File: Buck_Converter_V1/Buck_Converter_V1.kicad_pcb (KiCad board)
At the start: 2 copper layers, 75 x 40 mm, 28 parts, among them J1 Conn_01x01_Male, J2 Conn_01x01_Male, J3 Conn_01x01_Male, J4 Conn_01x01_Male, Q1 SI2319CDS-T1-GE3, U1 TL5001CDR

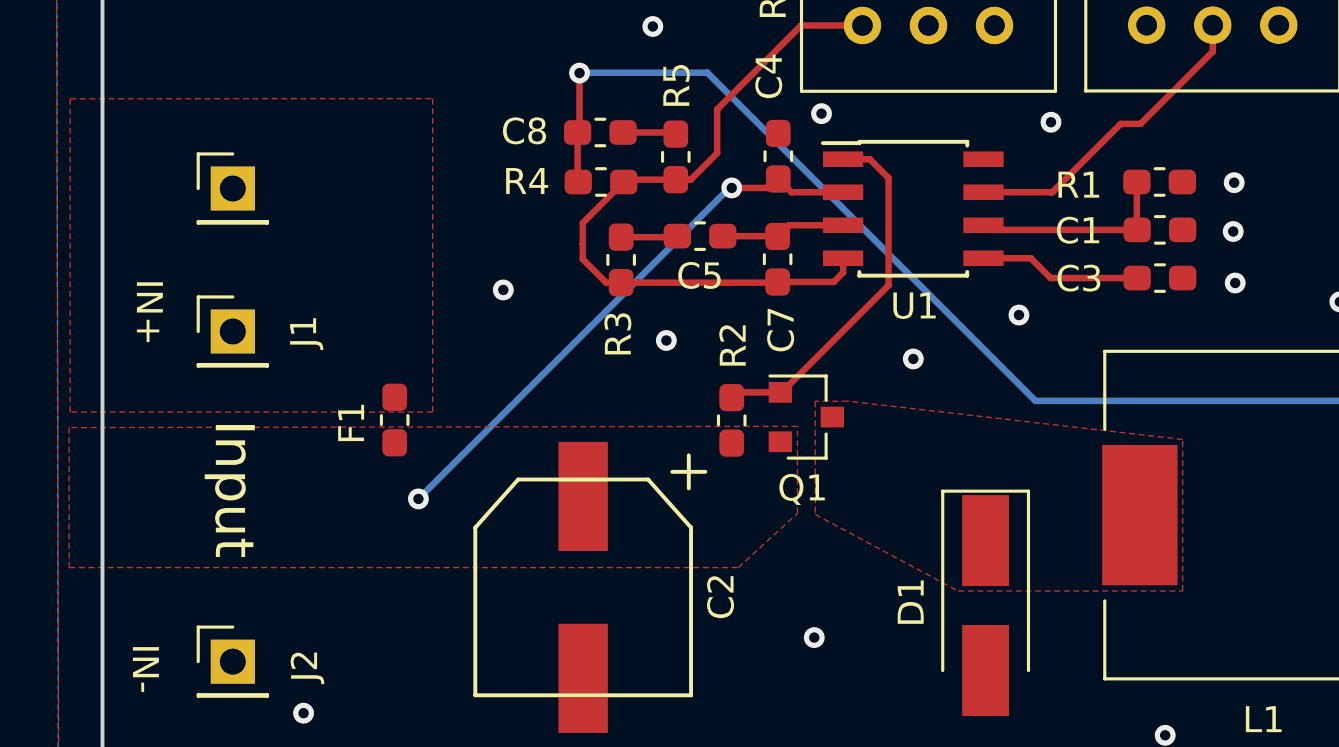
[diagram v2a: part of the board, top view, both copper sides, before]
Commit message: Changed footprint for PMOS switch. Generated gerber files.
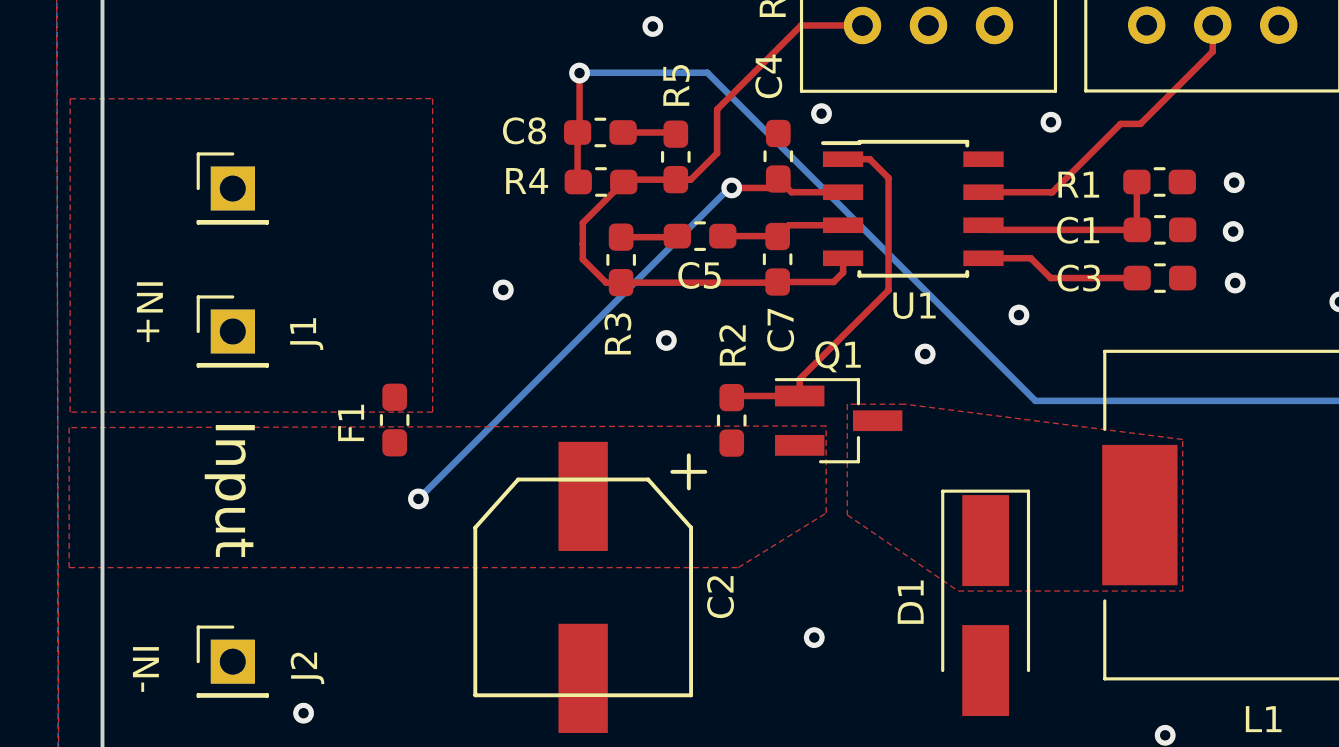
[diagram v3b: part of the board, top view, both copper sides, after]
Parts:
- Q1: footprint Package_TO_SOT_SMD:SOT-23 -> Package_TO_SOT_SMD:SOT-23_Handsoldering
- moved Q1 1.25 mm to (137.1, 89.2)
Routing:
- net P_DRIVE: track 14.0 -> 14.8 mm
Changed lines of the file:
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@@
     (thickness 1.6)
     (drawings 10)
-    (tracks 85)
+    (tracks 87)
     (zones 0)
     (modules 28)
@@
     (34 B.Paste user)
     (35 F.Paste user)
-    (36 B.SilkS user hide)
+    (36 B.SilkS user)
     (37 F.SilkS user)
     (38 B.Mask user)
@@
     (visible_elements FFFFFF7F)
     (pcbplotparams
-      (layerselection 0x010fc_ffffffff)
+      (layerselection 0x010f0_ffffffff)
       (usegerberextensions false)
       (usegerberattributes false)
@@
       (psa4output false)
       (plotreference true)
-      (plotvalue true)
+      (plotvalue false)
       (plotinvisibletext false)
       (padsonsilk false)
@@
       (outputformat 1)
       (mirror false)
-      (drillshape 1)
+      (drillshape 0)
       (scaleselection 1)
-      (outputdirectory ""))
+      (outputdirectory "Gerber/"))
   )
   (net 0 "")
@@
     )
   )
-  (module Package_TO_SOT_SMD:SOT-23 (layer F.Cu)
-    (at 135.8646 89.0905)
-    (descr "SOT-23, Standard")
-    (tags SOT-23)
-    (attr smd)
-    (fp_text reference Q1 (at -0.1397 2.7432 180) (layer F.SilkS)
-      (effects (font (size 1 1) (thickness 0.15)))
-    )
-    (fp_text value SI2319CDS-T1-GE3 (at 0 2.5) (layer F.Fab)
-      (effects (font (size 1 1) (thickness 0.15)))
-    )
-    (fp_text user %R (at 0 0 90) (layer F.Fab)
-      (effects (font (size 0.5 0.5) (thickness 0.075)))
-    )
-    (fp_line (start -0.7 -0.95) (end -0.7 1.5) (layer F.Fab) (width 0.1))
-    (fp_line (start -0.15 -1.52) (end 0.7 -1.52) (layer F.Fab) (width 0.1))
-    (fp_line (start -0.7 -0.95) (end -0.15 -1.52) (layer F.Fab) (width 0.1))
-    (fp_line (start 0.7 -1.52) (end 0.7 1.52) (layer F.Fab) (width 0.1))
-    (fp_line (start -0.7 1.52) (end 0.7 1.52) (layer F.Fab) (width 0.1))
-    (fp_line (start 0.76 1.58) (end 0.76 0.65) (layer F.SilkS) (width 0.12))
-    (fp_line (start 0.76 -1.58) (end 0.76 -0.65) (layer F.SilkS) (width 0.12))
-    (fp_line (start -1.7 -1.75) (end 1.7 -1.75) (layer F.CrtYd) (width 0.05))
-    (fp_line (start 1.7 -1.75) (end 1.7 1.75) (layer F.CrtYd) (width 0.05))
-    (fp_line (start 1.7 1.75) (end -1.7 1.75) (layer F.CrtYd) (width 0.05))
-    (fp_line (start -1.7 1.75) (end -1.7 -1.75) (layer F.CrtYd) (width 0.05))
-    (fp_line (start 0.76 -1.58) (end -1.4 -1.58) (layer F.SilkS) (width 0.12))
-    (fp_line (start 0.76 1.58) (end -0.7 1.58) (layer F.SilkS) (width 0.12))
-    (pad 1 smd rect (at -1 -0.95) (size 0.9 0.8) (layers F.Cu F.Paste F.Mask)
-      (net 12 P_DRIVE))
-    (pad 2 smd rect (at -1 0.95) (size 0.9 0.8) (layers F.Cu F.Paste F.Mask)
-      (net 3 Vin))
-    (pad 3 smd rect (at 1 0) (size 0.9 0.8) (layers F.Cu F.Paste F.Mask)
-      (net 10 "Net-(D1-Pad1)"))
-    (model ${KISYS3DMOD}/Package_TO_SOT_SMD.3dshapes/SOT-23.wrl
-      (at (xyz 0 0 0))
-      (scale (xyz 1 1 1))
-      (rotate (xyz 0 0 0))
-    )
-  )
   (module Resistor_SMD:R_0603_1608Metric_Pad1.05x0.95mm_HandSolder (layer F.Cu)
     (at 149.4536 80.0481)
@@
     )
   )
+  (module Package_TO_SOT_SMD:SOT-23_Handsoldering (layer F.Cu)
+    (at 137.1092 89.2302)
+    (descr "SOT-23, Handsoldering")
+    (tags SOT-23)
+    (attr smd)
+    (fp_text reference Q1 (at 0 -2.5) (layer F.SilkS)
+      (effects (font (size 1 1) (thickness 0.15)))
+    )
+    (fp_text value SI2319CDS-T1-GE3 (at 0 2.5) (layer F.Fab)
+      (effects (font (size 1 1) (thickness 0.15)))
+    )
+    (fp_text user %R (at 0 0 90) (layer F.Fab)
+      (effects (font (size 0.5 0.5) (thickness 0.075)))
+    )
+    (fp_line (start 0.76 1.58) (end 0.76 0.65) (layer F.SilkS) (width 0.12))
+    (fp_line (start 0.76 -1.58) (end 0.76 -0.65) (layer F.SilkS) (width 0.12))
+    (fp_line (start -2.7 -1.75) (end 2.7 -1.75) (layer F.CrtYd) (width 0.05))
+    (fp_line (start 2.7 -1.75) (end 2.7 1.75) (layer F.CrtYd) (width 0.05))
+    (fp_line (start 2.7 1.75) (end -2.7 1.75) (layer F.CrtYd) (width 0.05))
+    (fp_line (start -2.7 1.75) (end -2.7 -1.75) (layer F.CrtYd) (width 0.05))
+    (fp_line (start 0.76 -1.58) (end -2.4 -1.58) (layer F.SilkS) (width 0.12))
+    (fp_line (start -0.7 -0.95) (end -0.7 1.5) (layer F.Fab) (width 0.1))
+    (fp_line (start -0.15 -1.52) (end 0.7 -1.52) (layer F.Fab) (width 0.1))
+    (fp_line (start -0.7 -0.95) (end -0.15 -1.52) (layer F.Fab) (width 0.1))
+    (fp_line (start 0.7 -1.52) (end 0.7 1.52) (layer F.Fab) (width 0.1))
+    (fp_line (start -0.7 1.52) (end 0.7 1.52) (layer F.Fab) (width 0.1))
+    (fp_line (start 0.76 1.58) (end -0.7 1.58) (layer F.SilkS) (width 0.12))
+    (pad 1 smd rect (at -1.5 -0.95) (size 1.9 0.8) (layers F.Cu F.Paste F.Mask)
+      (net 12 P_DRIVE))
+    (pad 2 smd rect (at -1.5 0.95) (size 1.9 0.8) (layers F.Cu F.Paste F.Mask)
+      (net 3 Vin))
+    (pad 3 smd rect (at 1.5 0) (size 1.9 0.8) (layers F.Cu F.Paste F.Mask)
+      (net 10 "Net-(D1-Pad1)"))
+    (model ${KISYS3DMOD}/Package_TO_SOT_SMD.3dshapes/SOT-23.wrl
+      (at (xyz 0 0 0))
+      (scale (xyz 1 1 1))
+      (rotate (xyz 0 0 0))
+    )
+  )
   (gr_text "Min Vin = 3.6V\nMax Vin = 20V\nMax Iout = 3A" (at 146.558 88.0618 90) (layer B.SilkS)
     (effects (font (size 1.5 1.5) (thickness 0.3)) (justify mirror))
@@
   (via (at 124.206 84.201) (size 0.8) (drill 0.4) (layers F.Cu B.Cu) (net 2))
   (via (at 130.4798 86.1441) (size 0.8) (drill 0.4) (layers F.Cu B.Cu) (net 2))
-  (via (at 139.9794 86.8553) (size 0.8) (drill 0.4) (layers F.Cu B.Cu) (net 2))
+  (via (at 140.4366 86.6648) (size 0.8) (drill 0.4) (layers F.Cu B.Cu) (net 2))
   (via (at 144.0434 85.1662) (size 0.8) (drill 0.4) (layers F.Cu B.Cu) (net 2))
   (via (at 129.9591 74.0664) (size 0.8) (drill 0.4) (layers F.Cu B.Cu) (net 2))
@@
   (segment (start 130.778334 78.1431) (end 130.843134 78.2079) (width 0.25) (layer F.Cu) (net 9))
   (segment (start 128.8148 78.1431) (end 130.778334 78.1431) (width 0.25) (layer F.Cu) (net 9))
-  (segment (start 139.0269 84.0282) (end 134.9146 88.1405) (width 0.25) (layer F.Cu) (net 12))
   (segment (start 134.9146 88.1405) (end 134.8646 88.1405) (width 0.25) (layer F.Cu) (net 12))
-  (segment (start 139.0269 79.8943) (end 139.0269 84.0282) (width 0.25) (layer F.Cu) (net 12))
-  (segment (start 138.3044 79.1718) (end 139.0269 79.8943) (width 0.25) (layer F.Cu) (net 12))
-  (segment (start 137.2794 79.1718) (end 138.3044 79.1718) (width 0.25) (layer F.Cu) (net 12))
   (segment (start 133.1964 88.1405) (end 132.9944 88.3425) (width 0.25) (layer F.Cu) (net 12))
-  (segment (start 134.8646 88.1405) (end 133.1964 88.1405) (width 0.25) (layer F.Cu) (net 12))
+  (segment (start 138.3044 79.1718) (end 137.2794 79.1718) (width 0.25) (layer F.Cu) (net 12))
+  (segment (start 139.0269 84.2125) (end 139.0269 79.8943) (width 0.25) (layer F.Cu) (net 12))
+  (segment (start 135.6092 87.6302) (end 139.0269 84.2125) (width 0.25) (layer F.Cu) (net 12))
+  (segment (start 139.0269 79.8943) (end 138.3044 79.1718) (width 0.25) (layer F.Cu) (net 12))
+  (segment (start 135.6092 88.2802) (end 135.6092 87.6302) (width 0.25) (layer F.Cu) (net 12))
+  (segment (start 133.0567 88.2802) (end 132.9944 88.3425) (width 0.25) (layer F.Cu) (net 12))
+  (segment (start 135.6092 88.2802) (end 133.0567 88.2802) (width 0.25) (layer F.Cu) (net 12))
   (segment (start 142.6794 80.4418) (end 145.2499 80.4418) (width 0.25) (layer F.Cu) (net 13))
   (segment (start 145.2499 80.4418) (end 145.3261 80.4418) (width 0.25) (layer F.Cu) (net 13))
@@
     (polygon
       (pts
-        (xy 135.5217 89.4461) (xy 107.5055 89.4969) (xy 107.5055 94.8817) (xy 133.2484 94.8817) (xy 135.5217 92.7989)
+        (xy 136.6266 89.4334) (xy 107.5055 89.4969) (xy 107.5055 94.8817) (xy 133.2484 94.8817) (xy 136.6266 92.7862)
       )
     )
@@
     (polygon
       (pts
-        (xy 136.2075 88.4809) (xy 136.2075 92.837) (xy 141.7066 95.7834) (xy 150.3426 95.7834) (xy 150.3426 89.9541)
-        (xy 137.4648 88.4809)
+        (xy 137.4394 88.5952) (xy 137.4394 92.85605) (xy 141.7066 95.7834) (xy 150.3426 95.7834) (xy 150.3426 89.9541)
+        (xy 139.6492 88.5952)
       )
     )
